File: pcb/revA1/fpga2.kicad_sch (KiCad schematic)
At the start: 22 parts, among them J1 FPGA JTAG, U1 XC6SLX25-FTG256, U2 W25Q128JVS, X1 50 MHz

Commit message: revA1, WIP
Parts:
- removed TP12, TP13, TP14, TP15, TP16, TP17, TP18: TestPoint, TestPoint:TestPoint_Pad_D1.5mm, symbol Connector:TestPoint
- T1: renamed from TP8; value TestPoint -> TestPoint1
- renumbered TP9 to T5, TP10 to T6, TP11 to T7
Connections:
- net ~{ROMCS}: now reaches U1.M11 (IO_L2N_CMPMOSI_2)
- net ~{xIODOS} renamed ~{xNMI}
- no-connect marks 27 -> 26

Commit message: revA1
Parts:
- added T8: TestPoint, TestPoint:TestPoint_Pad_D1.5mm, symbol Connector:TestPoint
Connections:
- net xF: now reaches U1.M7 (IO_L31N_GCLK30_D15_2)
- net ~{xDOS}: no longer names the net of U1.P2 (IO_L33P_M3DQ12_3)
- net ~{xDOS}: now also T8.1
- no-connect marks 26 -> 25
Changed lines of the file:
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@@
 	)
 	(no_connect
-		(at 41.91 101.6)
-	)
-	(no_connect
 		(at 266.7 87.63)
 	)
@@
 	(wire
 		(pts
+			(xy 143.51 63.5) (xy 146.05 63.5)
+		)
+		(stroke
+			(width 0)
+			(type default)
+		)
+	)
+	(wire
+		(pts
 			(xy 218.44 143.51) (xy 223.52 143.51)
 		)
@@
 	(wire
 		(pts
-			(xy 143.51 106.68) (xy 146.05 106.68)
+			(xy 39.37 101.6) (xy 41.91 101.6)
 		)
 		(stroke
@@
 	(wire
 		(pts
-			(xy 143.51 50.8) (xy 146.05 50.8)
+			(xy 143.51 106.68) (xy 146.05 106.68)
 		)
 		(stroke
@@
 	(wire
 		(pts
-			(xy 39.37 68.58) (xy 41.91 68.58)
+			(xy 143.51 50.8) (xy 146.05 50.8)
 		)
 		(stroke
@@
 	(wire
 		(pts
-			(xy 243.84 33.02) (xy 246.38 33.02)
+			(xy 39.37 68.58) (xy 41.91 68.58)
 		)
 		(stroke
@@
 	(wire
 		(pts
-			(xy 143.51 63.5) (xy 146.05 63.5)
+			(xy 243.84 33.02) (xy 246.38 33.02)
 		)
 		(stroke
@@
 		)
 	)
+	(global_label "xF"
+		(shape input)
+		(at 39.37 101.6 180)
+		(fields_autoplaced yes)
+		(effects
+			(font
+				(size 0.9906 0.9906)
+			)
+			(justify right)
+		)
+		(property "Intersheetrefs" "${INTERSHEET_REFS}"
+			(at 35.3165 101.6 0)
+			(hide yes)
+			(show_name no)
+			(do_not_autoplace no)
+			(effects
+				(font
+					(size 0.9906 0.9906)
+				)
+				(justify right)
+			)
+		)
+	)
 	(global_label "VU_L2"
 		(shape input)
@@
 		)
 	)
-	(global_label "~{xDOS}"
-		(shape input)
-		(at 146.05 63.5 0)
-		(fields_autoplaced yes)
-		(effects
-			(font
-				(size 0.9906 0.9906)
-			)
-			(justify left)
-		)
-		(property "Intersheetrefs" "${INTERSHEET_REFS}"
-			(at 152.2262 63.5 0)
-			(hide yes)
-			(show_name no)
-			(do_not_autoplace no)
-			(effects
-				(font
-					(size 0.9906 0.9906)
-				)
-				(justify left)
-			)
-		)
-	)
 	(global_label "~{xM1}"
 		(shape input)
@@
 					(unit 1)
 				)
+			)
+		)
+	)
+	(symbol
+		(lib_id "Connector:TestPoint")
+		(at 146.05 63.5 270)
+		(unit 1)
+		(body_style 1)
+		(exclude_from_sim no)
+		(in_bom yes)
+		(on_board yes)
+		(in_pos_files yes)
+		(dnp no)
+		(property "Reference" "T8"
+			(at 152.4 63.5 90)
+			(show_name no)
+			(do_not_autoplace no)
+			(effects
+				(font
+					(size 0.9906 0.9906)
+				)
+			)
+		)
+		(property "Value" "TestPoint"
+			(at 148.0821 66.04 0)
+			(hide yes)
+			(show_name no)
+			(do_not_autoplace no)
+			(effects
+				(font
+					(size 0.9906 0.9906)
+				)
+				(justify left)
+			)
+		)
+		(property "Footprint" "TestPoint:TestPoint_Pad_D1.5mm"
+			(at 146.05 68.58 0)
+			(hide yes)
+			(show_name no)
+			(do_not_autoplace no)
+			(effects
+				(font
+					(size 1.27 1.27)
+				)
+			)
+		)
+		(property "Datasheet" ""
+			(at 146.05 68.58 0)
+			(hide yes)
+			(show_name no)
+			(do_not_autoplace no)
+			(effects
+				(font
+					(size 1.27 1.27)
+				)
+			)
+		)
+		(property "Description" "test point"
+			(at 146.05 63.5 0)
+			(hide yes)
+			(show_name no)
+			(do_not_autoplace no)
+			(effects
+				(font
+					(size 1.27 1.27)
+				)
+			)
+		)
+		(pin "1"
+		)
+		(instances
+			(project "karabas-megabuzz"
+				(path "/eff1afb7-47ba-46af-a815-4a07fb8d674b/e7252a15-61a8-4bf7-9e14-907719ec721b"
+					(reference "T8")
+					(unit 1)
+				)

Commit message: Small improvements to the revA1
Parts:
- JP1: now not fitted; now left out of the parts list
- T1, T5, T6, T7, T8: now left out of the parts list
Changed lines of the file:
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@@
 	(title_block
 		(title "Karabas-MegaBuzz")
-		(date "2026-05-27")
+		(date "2026-05-29")
 		(rev "A1")
 		(company "Andy Karpov")
@@
 		(body_style 1)
 		(exclude_from_sim no)
-		(in_bom yes)
+		(in_bom no)
 		(on_board yes)
 		(in_pos_files yes)
@@
 		(body_style 1)
 		(exclude_from_sim no)
-		(in_bom yes)
+		(in_bom no)
 		(on_board yes)
 		(in_pos_files yes)
@@
 		(body_style 1)
 		(exclude_from_sim no)
-		(in_bom yes)
+		(in_bom no)
 		(on_board yes)
 		(in_pos_files yes)
@@
 		(body_style 1)
 		(exclude_from_sim no)
-		(in_bom yes)
+		(in_bom no)
 		(on_board yes)
 		(in_pos_files yes)
@@
 		(body_style 1)
 		(exclude_from_sim no)
-		(in_bom yes)
+		(in_bom no)
 		(on_board yes)
 		(in_pos_files yes)
@@
 		(body_style 1)
 		(exclude_from_sim no)
-		(in_bom yes)
+		(in_bom no)
 		(on_board yes)
 		(in_pos_files yes)
-		(dnp no)
+		(dnp yes)
 		(property "Reference" "JP1"
 			(at 259.715 140.335 90)

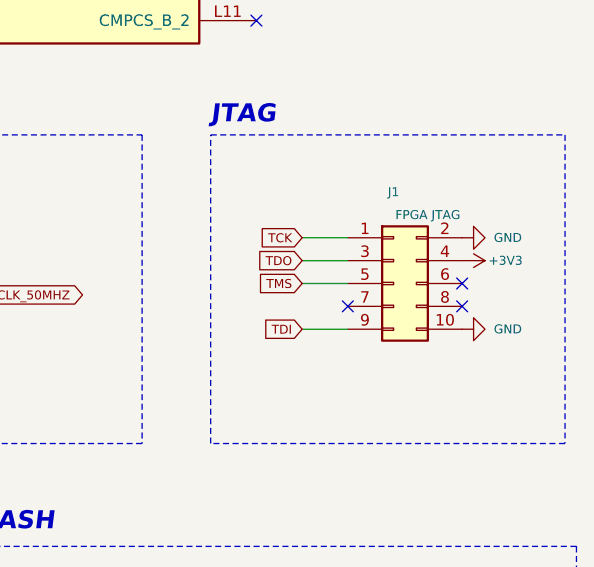
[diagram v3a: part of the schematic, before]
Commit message: Fixed missing LED1 connection, new revA1 release
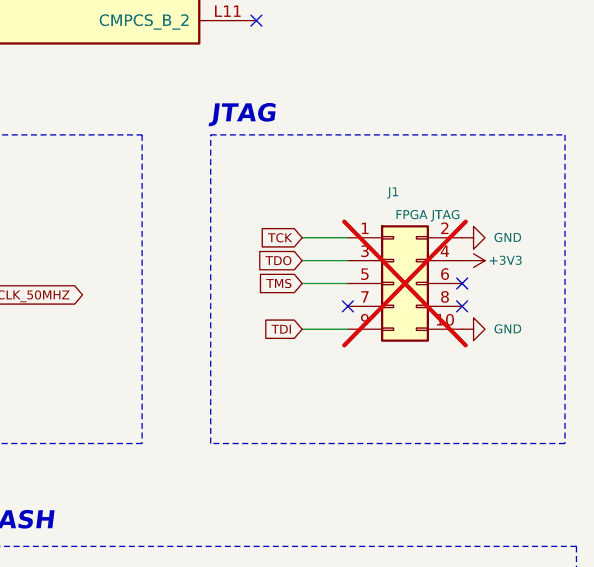
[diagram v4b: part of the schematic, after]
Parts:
- J1: now not fitted; now left out of the parts list
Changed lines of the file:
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@@
 		(body_style 1)
 		(exclude_from_sim no)
-		(in_bom yes)
+		(in_bom no)
 		(on_board yes)
 		(in_pos_files yes)
-		(dnp no)
+		(dnp yes)
 		(property "Reference" "J1"
 			(at 259.08 74.93 0)
